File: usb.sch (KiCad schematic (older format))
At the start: 8 parts, among them Q5 2N7002P, U16 NX5P3090UKZ

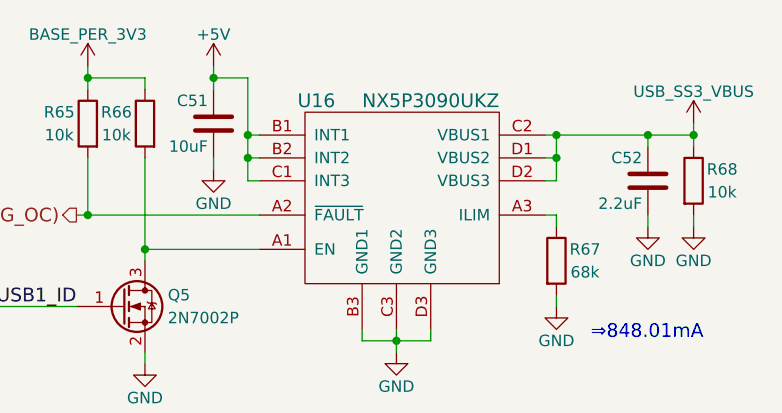
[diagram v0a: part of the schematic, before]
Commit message: Assign all associated signals to their respective pins on the EmCraft i.MX8M SoM
The ERC is now at the same state as the DART SoM schematic. Need to compare various aspects of the current schematic against the EmCraft reference design. The main buck-boost will likely need to be switched to a 5V regulator, or be configured to output 5V.

A regulator will likely need to be added which will output some VBAT voltage level (3.5~4.2V) for the M.2 cards. The SIM7100 for example requires at least 3.4V!
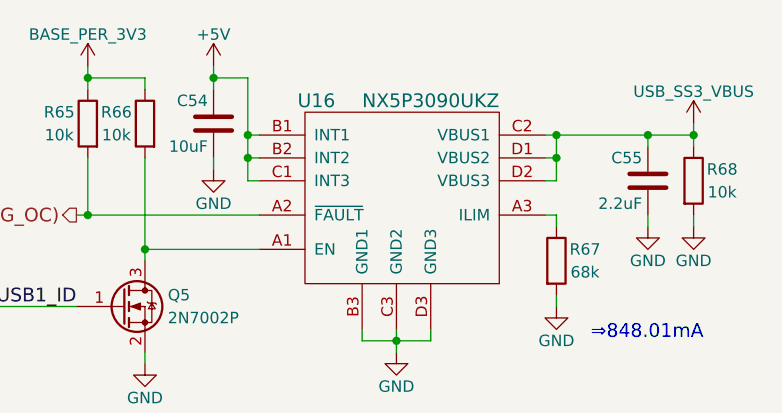
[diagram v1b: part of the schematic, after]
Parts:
- renumbered C51 to C54, C52 to C55
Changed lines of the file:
@@
 $EndComp
 $Comp
-L GND #PWR0126
+L GND #PWR0128
 U 1 1 5ACF654F
 P 6800 4100
-F 0 "#PWR0126" H 6800 3850 50  0001 C CNN
+F 0 "#PWR0128" H 6800 3850 50  0001 C CNN
 F 1 "GND" H 6800 3950 50  0000 C CNN
 F 2 "" H 6800 4100 50  0001 C CNN
@@
 $EndComp
 $Comp
-L C C51
+L C C54
 U 1 1 5ACBFFF9
 P 5300 3300
-F 0 "C51" H 5325 3400 50  0000 L CNN
+F 0 "C54" H 5325 3400 50  0000 L CNN
 F 1 "10uF" H 5325 3200 50  0000 L CNN
 F 2 "" H 5338 3150 50  0001 C CNN
@@
 $EndComp
 $Comp
-L C C52
+L C C55
 U 1 1 5ACC0253
 P 7200 3550
-F 0 "C52" H 7225 3650 50  0000 L CNN
+F 0 "C55" H 7225 3650 50  0000 L CNN
 F 1 "2.2uF" H 7225 3450 50  0000 L CNN
 F 2 "" H 7238 3400 50  0001 C CNN
@@
 $EndComp
 $Comp
-L GND #PWR0127
+L GND #PWR0129
 U 1 1 5ACC064A
 P 5300 3500
-F 0 "#PWR0127" H 5300 3250 50  0001 C CNN
+F 0 "#PWR0129" H 5300 3250 50  0001 C CNN
 F 1 "GND" H 5300 3350 50  0000 C CNN
 F 2 "" H 5300 3500 50  0001 C CNN
@@
 Connection ~ 5450 3350
 $Comp
-L +5V #PWR0128
+L +5V #PWR0130
 U 1 1 5ACC0801
 P 5300 3050
-F 0 "#PWR0128" H 5300 2900 50  0001 C CNN
+F 0 "#PWR0130" H 5300 2900 50  0001 C CNN
 F 1 "+5V" H 5300 3190 50  0000 C CNN
 F 2 "" H 5300 3050 50  0001 C CNN
@@
 GPIO1_IO13(USB1_OTG_OC)
 $Comp
-L BASE_PER_3V3 #PWR0129
+L BASE_PER_3V3 #PWR0131
 U 1 1 5ACC0CDC
 P 4750 3050
-F 0 "#PWR0129" H 4750 2900 50  0001 C CNN
+F 0 "#PWR0131" H 4750 2900 50  0001 C CNN
 F 1 "BASE_PER_3V3" H 4750 3190 50  0000 C CNN
 F 2 "" H 4750 3050 50  0001 C CNN
@@
 	4350 4100 4700 4100
 $Comp
-L GND #PWR0130
+L GND #PWR0132
 U 1 1 5ACC18BD
 P 5000 4350
-F 0 "#PWR0130" H 5000 4100 50  0001 C CNN
+F 0 "#PWR0132" H 5000 4100 50  0001 C CNN
 F 1 "GND" H 5000 4200 50  0000 C CNN
 F 2 "" H 5000 4350 50  0001 C CNN
@@
 	5000 4350 5000 4300
 $Comp
-L GND #PWR0131
+L GND #PWR0133
 U 1 1 5ACC1A19
 P 6100 4300
-F 0 "#PWR0131" H 6100 4050 50  0001 C CNN
+F 0 "#PWR0133" H 6100 4050 50  0001 C CNN
 F 1 "GND" H 6100 4150 50  0000 C CNN
 F 2 "" H 6100 4300 50  0001 C CNN
@@
 Connection ~ 6100 4250
 $Comp
-L GND #PWR0132
+L GND #PWR0134
 U 1 1 5ACC1F9D
 P 7200 3750
-F 0 "#PWR0132" H 7200 3500 50  0001 C CNN
+F 0 "#PWR0134" H 7200 3500 50  0001 C CNN
 F 1 "GND" H 7200 3600 50  0000 C CNN
 F 2 "" H 7200 3750 50  0001 C CNN
@@
 Connection ~ 7400 3350
 $Comp
-L GND #PWR0133
+L GND #PWR0135
 U 1 1 5ACC294F
 P 7400 3750
-F 0 "#PWR0133" H 7400 3500 50  0001 C CNN
+F 0 "#PWR0135" H 7400 3500 50  0001 C CNN
 F 1 "GND" H 7400 3600 50  0000 C CNN
 F 2 "" H 7400 3750 50  0001 C CNN
@@
 	7400 3700 7400 3750
 $Comp
-L USB_SS3_VBUS #PWR0134
+L USB_SS3_VBUS #PWR0136
 U 1 1 5ACC617E
 P 7400 3300
-F 0 "#PWR0134" H 7400 3150 50  0001 C CNN
+F 0 "#PWR0136" H 7400 3150 50  0001 C CNN
 F 1 "USB_SS3_VBUS" H 7400 3440 50  0000 C CNN
 F 2 "" H 7400 3300 50  0001 C CNN

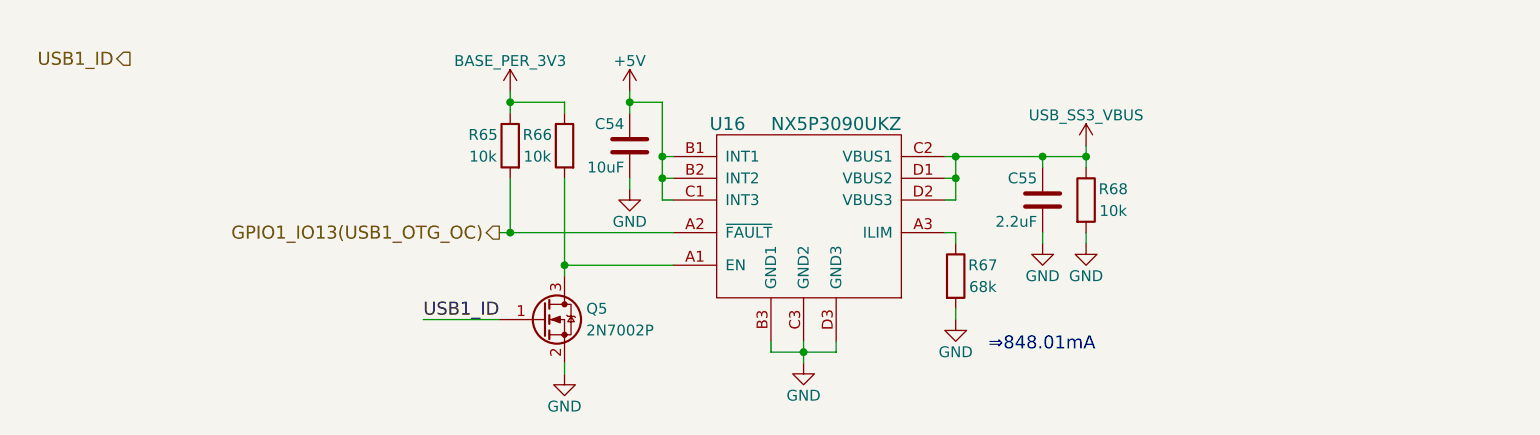
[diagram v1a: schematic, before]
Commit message: Use "Start to sheet number*100 and use first free number" designation, any new component added to the schematic will occupy the next available number in that sheet
For example: if sheet 2 has R201-R215 and we add a new resistor it will become R216.
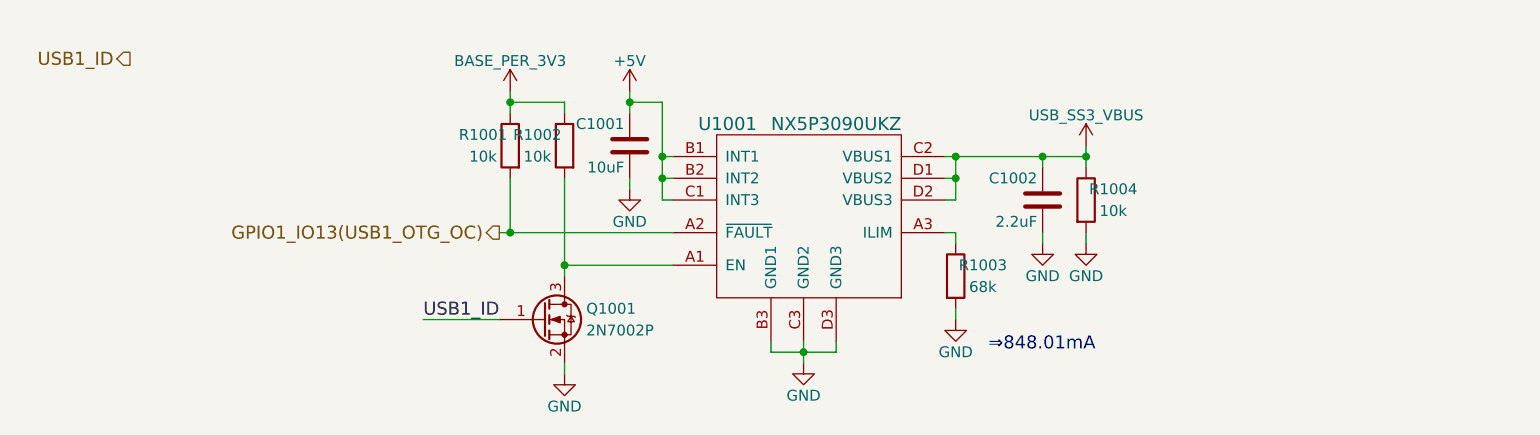
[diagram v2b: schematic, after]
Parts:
- renumbered C54 to C1001, C55 to C1002, Q5 to Q1001, R65 to R1001, R66 to R1002, R67 to R1003, R68 to R1004, U16 to U1001
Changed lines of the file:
@@
 $EndDescr
 $Comp
-L NX5P3090UKZ U16
+L NX5P3090UKZ U1001
 U 1 1 5ACF2C5E
 P 6100 3600
-F 0 "U16" H 5750 4000 60  0000 C CNN
+F 0 "U1001" H 5750 4000 60  0000 C CNN
 F 1 "NX5P3090UKZ" H 6250 4000 60  0000 C CNN
 F 2 "" H 6100 3600 60  0001 C CNN
@@
 $EndComp
 $Comp
-L R R67
+L R R1003
 U 1 1 5ACF5CFA
 P 6800 3900
-F 0 "R67" H 6925 3950 50  0000 C CNN
+F 0 "R1003" H 6925 3950 50  0000 C CNN
 F 1 "68k" H 6925 3850 50  0000 C CNN
 F 2 "" V 6730 3900 50  0001 C CNN
@@
 $EndComp
 $Comp
-L GND #PWR0128
+L GND #PWR1006
 U 1 1 5ACF654F
 P 6800 4100
-F 0 "#PWR0128" H 6800 3850 50  0001 C CNN
+F 0 "#PWR1006" H 6800 3850 50  0001 C CNN
 F 1 "GND" H 6800 3950 50  0000 C CNN
 F 2 "" H 6800 4100 50  0001 C CNN
@@
 ⇒848.01mA
 $Comp
-L R R65
+L R R1001
 U 1 1 5ACBFFBD
 P 4750 3300
-F 0 "R65" H 4875 3350 50  0000 C CNN
+F 0 "R1001" H 4875 3350 50  0000 C CNN
 F 1 "10k" H 4875 3250 50  0000 C CNN
 F 2 "" V 4680 3300 50  0001 C CNN
@@
 $EndComp
 $Comp
-L R R66
+L R R1002
 U 1 1 5ACBFFD9
 P 5000 3300
-F 0 "R66" H 5125 3350 50  0000 C CNN
+F 0 "R1002" H 5125 3350 50  0000 C CNN
 F 1 "10k" H 5125 3250 50  0000 C CNN
 F 2 "" V 4930 3300 50  0001 C CNN
@@
 $EndComp
 $Comp
-L C C54
+L C C1001
 U 1 1 5ACBFFF9
 P 5300 3300
-F 0 "C54" H 5325 3400 50  0000 L CNN
+F 0 "C1001" H 5325 3400 50  0000 L CNN
 F 1 "10uF" H 5325 3200 50  0000 L CNN
 F 2 "" H 5338 3150 50  0001 C CNN
@@
 $EndComp
 $Comp
-L Q_NMOS_GSD Q5
+L Q_NMOS_GSD Q1001
 U 1 1 5ACC004D
 P 4900 4100
-F 0 "Q5" H 5100 4150 50  0000 L CNN
+F 0 "Q1001" H 5100 4150 50  0000 L CNN
 F 1 "2N7002P" H 5100 4050 50  0000 L CNN
 F 2 "" H 5100 4200 50  0001 C CNN
@@
 $EndComp
 $Comp
-L C C55
+L C C1002
 U 1 1 5ACC0253
 P 7200 3550
-F 0 "C55" H 7225 3650 50  0000 L CNN
+F 0 "C1002" H 7225 3650 50  0000 L CNN
 F 1 "2.2uF" H 7225 3450 50  0000 L CNN
 F 2 "" H 7238 3400 50  0001 C CNN
@@
 $EndComp
 $Comp
-L R R68
+L R R1004
 U 1 1 5ACC03AD
 P 7400 3550
-F 0 "R68" H 7525 3600 50  0000 C CNN
+F 0 "R1004" H 7525 3600 50  0000 C CNN
 F 1 "10k" H 7525 3500 50  0000 C CNN
 F 2 "" V 7330 3550 50  0001 C CNN
@@
 $EndComp
 $Comp
-L GND #PWR0129
+L GND #PWR1004
 U 1 1 5ACC064A
 P 5300 3500
-F 0 "#PWR0129" H 5300 3250 50  0001 C CNN
+F 0 "#PWR1004" H 5300 3250 50  0001 C CNN
 F 1 "GND" H 5300 3350 50  0000 C CNN
 F 2 "" H 5300 3500 50  0001 C CNN
@@
 Connection ~ 5450 3350
 $Comp
-L +5V #PWR0130
+L +5V #PWR1003
 U 1 1 5ACC0801
 P 5300 3050
-F 0 "#PWR0130" H 5300 2900 50  0001 C CNN
+F 0 "#PWR1003" H 5300 2900 50  0001 C CNN
 F 1 "+5V" H 5300 3190 50  0000 C CNN
 F 2 "" H 5300 3050 50  0001 C CNN
@@
 GPIO1_IO13(USB1_OTG_OC)
 $Comp
-L BASE_PER_3V3 #PWR0131
+L BASE_PER_3V3 #PWR1001
 U 1 1 5ACC0CDC
 P 4750 3050
-F 0 "#PWR0131" H 4750 2900 50  0001 C CNN
+F 0 "#PWR1001" H 4750 2900 50  0001 C CNN
 F 1 "BASE_PER_3V3" H 4750 3190 50  0000 C CNN
 F 2 "" H 4750 3050 50  0001 C CNN
@@
 	4350 4100 4700 4100
 $Comp
-L GND #PWR0132
+L GND #PWR1002
 U 1 1 5ACC18BD
 P 5000 4350
-F 0 "#PWR0132" H 5000 4100 50  0001 C CNN
+F 0 "#PWR1002" H 5000 4100 50  0001 C CNN
 F 1 "GND" H 5000 4200 50  0000 C CNN
 F 2 "" H 5000 4350 50  0001 C CNN
@@
 	5000 4350 5000 4300
 $Comp
-L GND #PWR0133
+L GND #PWR1005
 U 1 1 5ACC1A19
 P 6100 4300
-F 0 "#PWR0133" H 6100 4050 50  0001 C CNN
+F 0 "#PWR1005" H 6100 4050 50  0001 C CNN
 F 1 "GND" H 6100 4150 50  0000 C CNN
 F 2 "" H 6100 4300 50  0001 C CNN
@@
 Connection ~ 6100 4250
 $Comp
-L GND #PWR0134
+L GND #PWR1007
 U 1 1 5ACC1F9D
 P 7200 3750
-F 0 "#PWR0134" H 7200 3500 50  0001 C CNN
+F 0 "#PWR1007" H 7200 3500 50  0001 C CNN
 F 1 "GND" H 7200 3600 50  0000 C CNN
 F 2 "" H 7200 3750 50  0001 C CNN
@@
 Connection ~ 7400 3350
 $Comp
-L GND #PWR0135
+L GND #PWR1009
 U 1 1 5ACC294F
 P 7400 3750
-F 0 "#PWR0135" H 7400 3500 50  0001 C CNN
+F 0 "#PWR1009" H 7400 3500 50  0001 C CNN
 F 1 "GND" H 7400 3600 50  0000 C CNN
 F 2 "" H 7400 3750 50  0001 C CNN
@@
 	7400 3700 7400 3750
 $Comp
-L USB_SS3_VBUS #PWR0136
+L USB_SS3_VBUS #PWR1008
 U 1 1 5ACC617E
 P 7400 3300
-F 0 "#PWR0136" H 7400 3150 50  0001 C CNN
+F 0 "#PWR1008" H 7400 3150 50  0001 C CNN
 F 1 "USB_SS3_VBUS" H 7400 3440 50  0000 C CNN
 F 2 "" H 7400 3300 50  0001 C CNN

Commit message: Move reference designators in the schematic so that they are legible
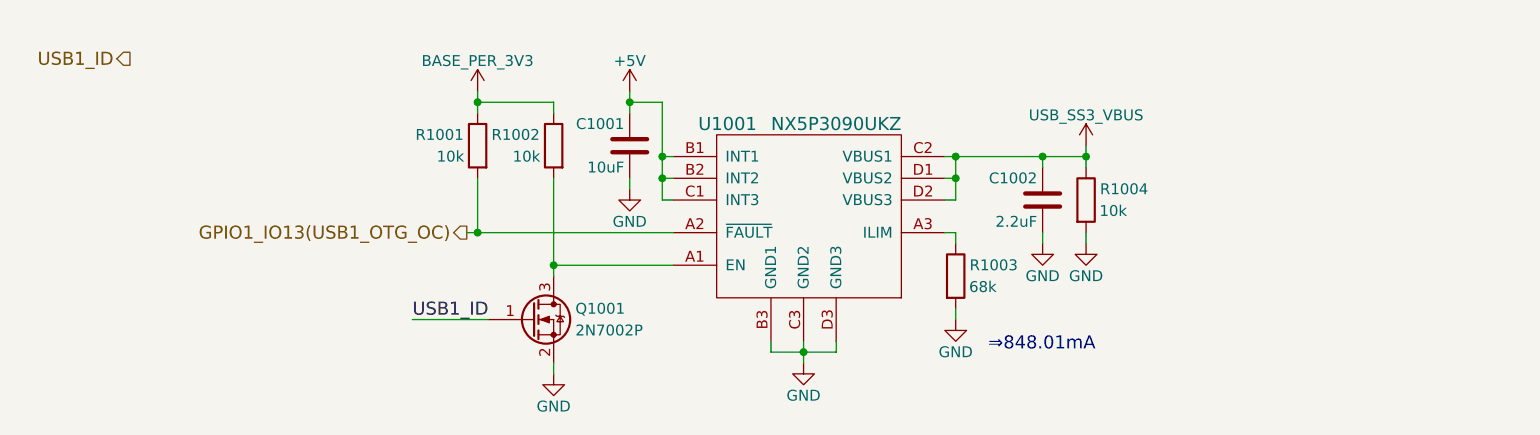
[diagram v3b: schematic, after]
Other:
- moved on the sheet: Q1001, R1001, R1002
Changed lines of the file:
@@
 U 1 1 5ACF5CFA
 P 6800 3900
-F 0 "R1003" H 6925 3950 50  0000 C CNN
+F 0 "R1003" H 6975 3950 50  0000 C CNN
 F 1 "68k" H 6925 3850 50  0000 C CNN
 F 2 "" V 6730 3900 50  0001 C CNN
@@
 $EndComp
 $Comp
-L GND #PWR1006
+L GND #PWR0128
 U 1 1 5ACF654F
 P 6800 4100
-F 0 "#PWR1006" H 6800 3850 50  0001 C CNN
+F 0 "#PWR0128" H 6800 3850 50  0001 C CNN
 F 1 "GND" H 6800 3950 50  0000 C CNN
 F 2 "" H 6800 4100 50  0001 C CNN
@@
 L R R1001
 U 1 1 5ACBFFBD
-P 4750 3300
-F 0 "R1001" H 4875 3350 50  0000 C CNN
-F 1 "10k" H 4875 3250 50  0000 C CNN
-F 2 "" V 4680 3300 50  0001 C CNN
-F 3 "" H 4750 3300 50  0001 C CNN
-	1    4750 3300
+P 4600 3300
+F 0 "R1001" H 4775 3350 50  0000 C CNN
+F 1 "10k" H 4725 3250 50  0000 C CNN
+F 2 "" V 4530 3300 50  0001 C CNN
+F 3 "" H 4600 3300 50  0001 C CNN
+	1    4600 3300
 	-1   0    0    -1
 $EndComp
@@
 L R R1002
 U 1 1 5ACBFFD9
-P 5000 3300
+P 4950 3300
 F 0 "R1002" H 5125 3350 50  0000 C CNN
-F 1 "10k" H 5125 3250 50  0000 C CNN
-F 2 "" V 4930 3300 50  0001 C CNN
-F 3 "" H 5000 3300 50  0001 C CNN
-	1    5000 3300
+F 1 "10k" H 5075 3250 50  0000 C CNN
+F 2 "" V 4880 3300 50  0001 C CNN
+F 3 "" H 4950 3300 50  0001 C CNN
+	1    4950 3300
 	-1   0    0    -1
 $EndComp
@@
 L Q_NMOS_GSD Q1001
 U 1 1 5ACC004D
-P 4900 4100
-F 0 "Q1001" H 5100 4150 50  0000 L CNN
-F 1 "2N7002P" H 5100 4050 50  0000 L CNN
-F 2 "" H 5100 4200 50  0001 C CNN
-F 3 "" H 4900 4100 50  0001 C CNN
-	1    4900 4100
+P 4850 4100
+F 0 "Q1001" H 5050 4150 50  0000 L CNN
+F 1 "2N7002P" H 5050 4050 50  0000 L CNN
+F 2 "" H 5050 4200 50  0001 C CNN
+F 3 "" H 4850 4100 50  0001 C CNN
+	1    4850 4100
 	1    0    0    -1
 $EndComp
@@
 U 1 1 5ACC03AD
 P 7400 3550
-F 0 "R1004" H 7525 3600 50  0000 C CNN
+F 0 "R1004" H 7575 3600 50  0000 C CNN
 F 1 "10k" H 7525 3500 50  0000 C CNN
 F 2 "" V 7330 3550 50  0001 C CNN
@@
 $EndComp
 $Comp
-L GND #PWR1004
+L GND #PWR0129
 U 1 1 5ACC064A
 P 5300 3500
-F 0 "#PWR1004" H 5300 3250 50  0001 C CNN
+F 0 "#PWR0129" H 5300 3250 50  0001 C CNN
 F 1 "GND" H 5300 3350 50  0000 C CNN
 F 2 "" H 5300 3500 50  0001 C CNN
@@
 	5450 3550 5500 3550
 Wire Wire Line
-	5450 3100 5450 3550
+	5450 3100 5450 3350
+Wire Wire Line
+	5450 3350 5450 3450
+Wire Wire Line
+	5450 3450 5450 3550
 Wire Wire Line
 	5450 3100 5300 3100
 Wire Wire Line
-	5300 3050 5300 3150
+	5300 3050 5300 3100
+Wire Wire Line
+	5300 3100 5300 3150
 Wire Wire Line
 	5500 3450 5450 3450
@@
 Connection ~ 5450 3350
 $Comp
-L +5V #PWR1003
+L +5V #PWR0130
 U 1 1 5ACC0801
 P 5300 3050
-F 0 "#PWR1003" H 5300 2900 50  0001 C CNN
+F 0 "#PWR0130" H 5300 2900 50  0001 C CNN
 F 1 "+5V" H 5300 3190 50  0000 C CNN
 F 2 "" H 5300 3050 50  0001 C CNN
@@
 $EndComp
 Connection ~ 5300 3100
-Text HLabel 4700 3700 0    60   Output ~ 0
+Text HLabel 4550 3700 0    60   Output ~ 0
 GPIO1_IO13(USB1_OTG_OC)
 $Comp
-L BASE_PER_3V3 #PWR1001
+L BASE_PER_3V3 #PWR0131
 U 1 1 5ACC0CDC
-P 4750 3050
-F 0 "#PWR1001" H 4750 2900 50  0001 C CNN
-F 1 "BASE_PER_3V3" H 4750 3190 50  0000 C CNN
-F 2 "" H 4750 3050 50  0001 C CNN
-F 3 "" H 4750 3050 50  0001 C CNN
-	1    4750 3050
-	1    0    0    -1
-$EndComp
-Wire Wire Line
-	4750 3050 4750 3150
-Wire Wire Line
-	5000 3150 5000 3100
-Wire Wire Line
-	5000 3100 4750 3100
-Connection ~ 4750 3100
-Wire Wire Line
-	4700 3700 5500 3700
-Wire Wire Line
-	4750 3450 4750 3700
-Connection ~ 4750 3700
-Wire Wire Line
-	5500 3850 5000 3850
-Wire Wire Line
-	5000 3450 5000 3900
-Connection ~ 5000 3850
-Wire Wire Line
-	4350 4100 4700 4100
-$Comp
-L GND #PWR1002
+P 4600 3050
+F 0 "#PWR0131" H 4600 2900 50  0001 C CNN
+F 1 "BASE_PER_3V3" H 4600 3190 50  0000 C CNN
+F 2 "" H 4600 3050 50  0001 C CNN
+F 3 "" H 4600 3050 50  0001 C CNN
+	1    4600 3050
+	1    0    0    -1
+$EndComp
+Wire Wire Line
+	4600 3050 4600 3100
+Wire Wire Line
+	4600 3100 4600 3150
+Wire Wire Line
+	4950 3150 4950 3100
+Wire Wire Line
+	4950 3100 4600 3100
+Connection ~ 4600 3100
+Wire Wire Line
+	4550 3700 4600 3700
+Wire Wire Line
+	4600 3700 5500 3700
+Wire Wire Line
+	4600 3450 4600 3700
+Connection ~ 4600 3700
+Wire Wire Line
+	5500 3850 4950 3850
+Wire Wire Line
+	4950 3450 4950 3850
+Wire Wire Line
+	4950 3850 4950 3900
+Connection ~ 4950 3850
+Wire Wire Line
+	4300 4100 4650 4100
+$Comp
+L GND #PWR0132
 U 1 1 5ACC18BD
-P 5000 4350
-F 0 "#PWR1002" H 5000 4100 50  0001 C CNN
-F 1 "GND" H 5000 4200 50  0000 C CNN
-F 2 "" H 5000 4350 50  0001 C CNN
-F 3 "" H 5000 4350 50  0001 C CNN
-	1    5000 4350
-	1    0    0    -1
-$EndComp
-Wire Wire Line
-	5000 4350 5000 4300
-$Comp
-L GND #PWR1005
+P 4950 4350
+F 0 "#PWR0132" H 4950 4100 50  0001 C CNN
+F 1 "GND" H 4950 4200 50  0000 C CNN
+F 2 "" H 4950 4350 50  0001 C CNN
+F 3 "" H 4950 4350 50  0001 C CNN
+	1    4950 4350
+	1    0    0    -1
+$EndComp
+Wire Wire Line
+	4950 4350 4950 4300
+$Comp
+L GND #PWR0133
 U 1 1 5ACC1A19
 P 6100 4300
-F 0 "#PWR1005" H 6100 4050 50  0001 C CNN
+F 0 "#PWR0133" H 6100 4050 50  0001 C CNN
 F 1 "GND" H 6100 4150 50  0000 C CNN
 F 2 "" H 6100 4300 50  0001 C CNN
@@
 	5950 4200 5950 4250
 Wire Wire Line
-	5950 4250 6250 4250
+	5950 4250 6100 4250
+Wire Wire Line
+	6100 4250 6250 4250
 Wire Wire Line
 	6250 4250 6250 4200
 Wire Wire Line
-	6100 4200 6100 4300
+	6100 4200 6100 4250
+Wire Wire Line
+	6100 4250 6100 4300
 Connection ~ 6100 4250
 $Comp
-L GND #PWR1007
+L GND #PWR0134
 U 1 1 5ACC1F9D
 P 7200 3750
-F 0 "#PWR1007" H 7200 3500 50  0001 C CNN
+F 0 "#PWR0134" H 7200 3500 50  0001 C CNN
 F 1 "GND" H 7200 3600 50  0000 C CNN
 F 2 "" H 7200 3750 50  0001 C CNN
@@
 $EndComp
 Wire Wire Line
-	6750 3350 7400 3350
-Wire Wire Line
-	7400 3300 7400 3400
+	6750 3350 6800 3350
+Wire Wire Line
+	6800 3350 7200 3350
+Wire Wire Line
+	7200 3350 7400 3350
+Wire Wire Line
+	7400 3300 7400 3350
+Wire Wire Line
+	7400 3350 7400 3400
 Wire Wire Line
 	6800 3550 6750 3550
 Wire Wire Line
-	6800 3350 6800 3550
+	6800 3350 6800 3450
+Wire Wire Line
+	6800 3450 6800 3550
 Connection ~ 6800 3350
 Wire Wire Line
@@
 Connection ~ 7400 3350
 $Comp
-L GND #PWR1009
+L GND #PWR0135
 U 1 1 5ACC294F
 P 7400 3750
-F 0 "#PWR1009" H 7400 3500 50  0001 C CNN
+F 0 "#PWR0135" H 7400 3500 50  0001 C CNN
 F 1 "GND" H 7400 3600 50  0000 C CNN
 F 2 "" H 7400 3750 50  0001 C CNN
@@
 	7400 3700 7400 3750
 $Comp
-L USB_SS3_VBUS #PWR1008
+L USB_SS3_VBUS #PWR0136
 U 1 1 5ACC617E
 P 7400 3300
-F 0 "#PWR1008" H 7400 3150 50  0001 C CNN
+F 0 "#PWR0136" H 7400 3150 50  0001 C CNN
 F 1 "USB_SS3_VBUS" H 7400 3440 50  0000 C CNN
 F 2 "" H 7400 3300 50  0001 C CNN
@@
 	1    0    0    -1
 $EndComp
-Text Label 4350 4100 0    60   ~ 0
+Text Label 4300 4100 0    60   ~ 0
 USB1_ID
 Text HLabel 3000 2900 0    60   Output ~ 0

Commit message: Include reverse polarity protection circuit along with a simulation showing its effectiveness
Protecting VBAT from when board is sinking current via USB C. Protects against reverse polarity at the DC jack.

In EmCraft's instance VBUS should only be 5V when sinking current but they must protect against the condition when VBUS>12V and DC_IN=12V. This may need testing.
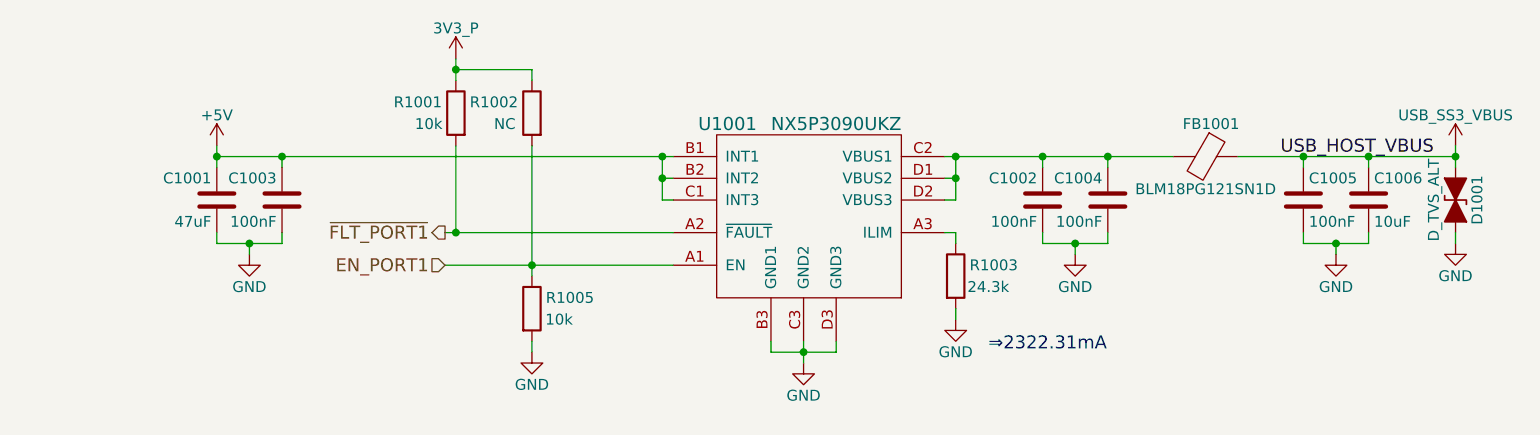
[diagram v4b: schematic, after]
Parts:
- removed Q1001: 2N7002P, symbol Q_NMOS_GSD
- removed R1004: 10k, symbol R
- added C1003, C1004, C1005: 100nF, symbol C
- added C1006: 10uF, symbol C
- added D1001: D_TVS_ALT, symbol D_TVS_ALT
- added FB1001: BLM18PG121SN1D, symbol Ferrite_Bead
- added R1005: 10k, symbol R
- C1001: value 10uF -> 47uF
- C1002: value 2.2uF -> 100nF
- R1002: value 10k -> NC
- R1003: value 68k -> 24.3k
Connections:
- net +5V: now also C1003.1
- net GND: now also C1003.2, C1004.2, C1005.2, C1006.2, D1001.2 (A2), R1005.2
- net USB_SS3_VBUS: now also C1005.1, C1006.1, D1001.1 (A1), FB1001.1; no longer C1002.1, U1001.C2 (VBUS1), U1001.D1 (VBUS2), U1001.D2 (VBUS3)
- net EN_PORT1: now reaches R1002.2, U1001.A1 (EN)
- net EN_PORT1: now also R1005.1
- net BASE_PER_3V3 renamed 3V3_P
- net GPIO1_IO13(USB1_OTG_OC) renamed ~FLT_PORT1
- new net: C1002.1, C1004.1, FB1001.2, U1001.C2 (VBUS1), U1001.D1 (VBUS2), U1001.D2 (VBUS3)
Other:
- note added: "⇒2322.31mA"
- note removed: "⇒848.01mA"
- moved on the sheet: C1001, R1001, R1002
